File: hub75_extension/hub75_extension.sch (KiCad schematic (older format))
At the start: 23 parts

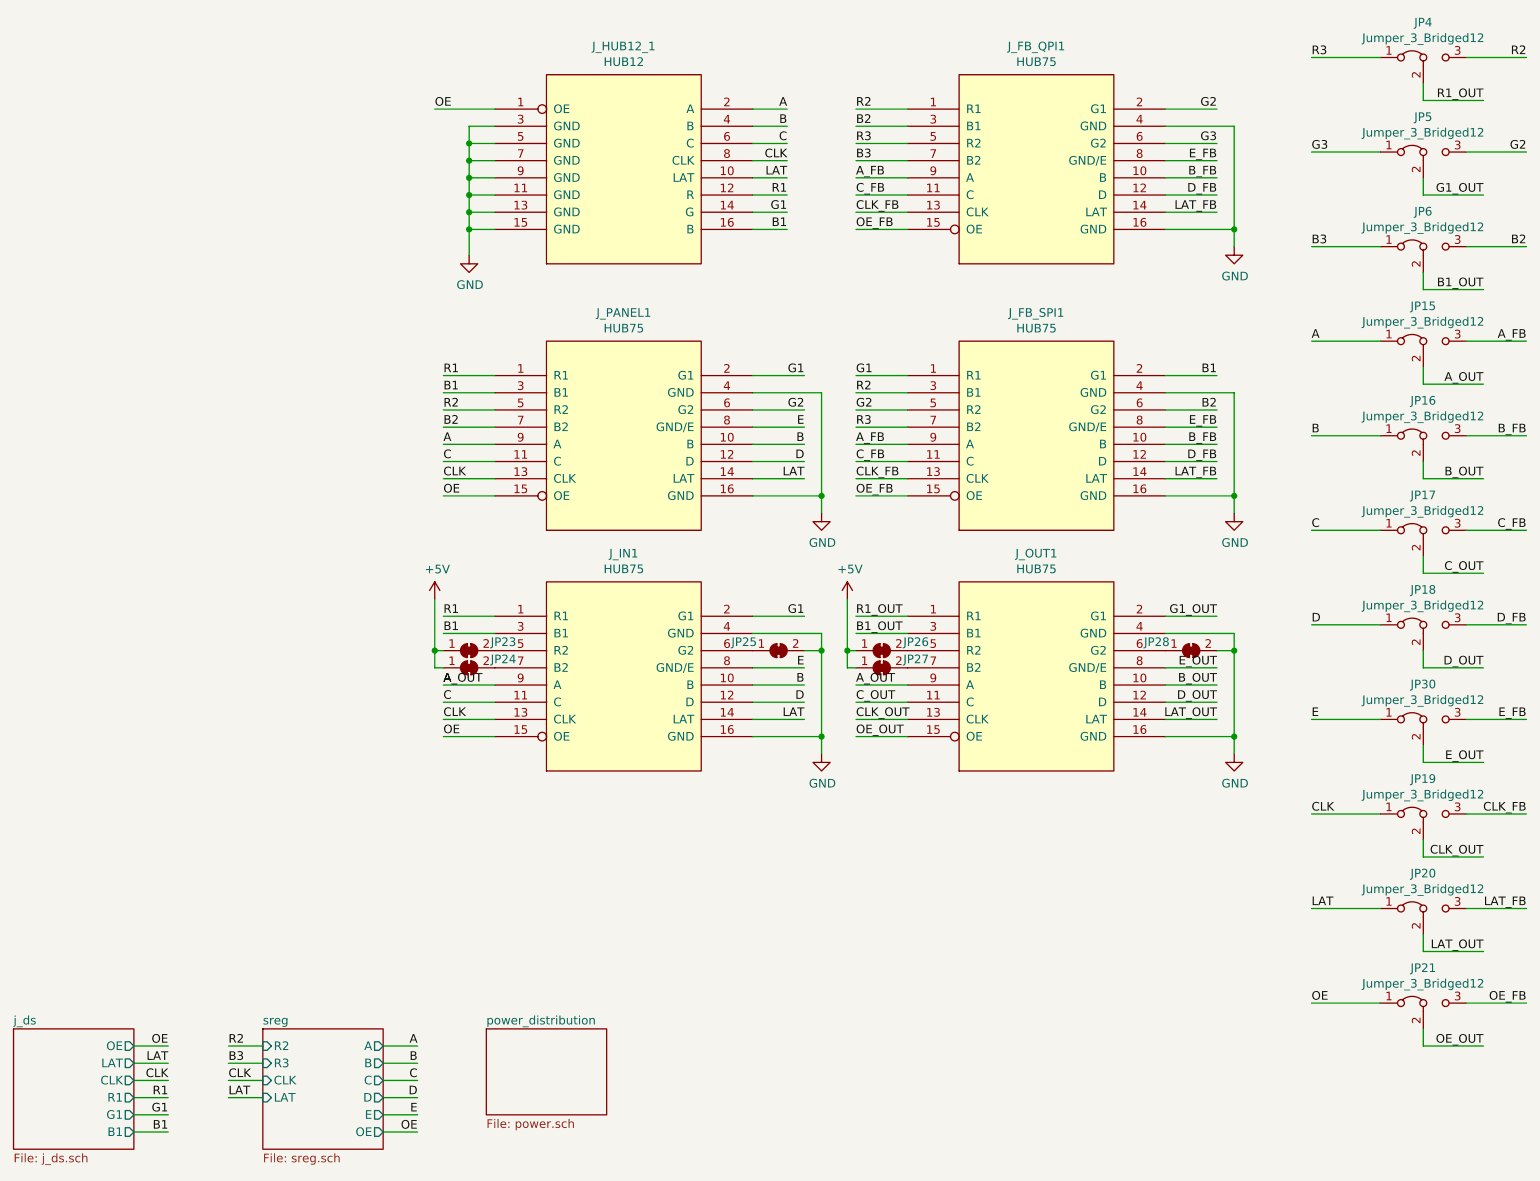
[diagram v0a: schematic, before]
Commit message: Refactor HUB75 connectors to their own sheet
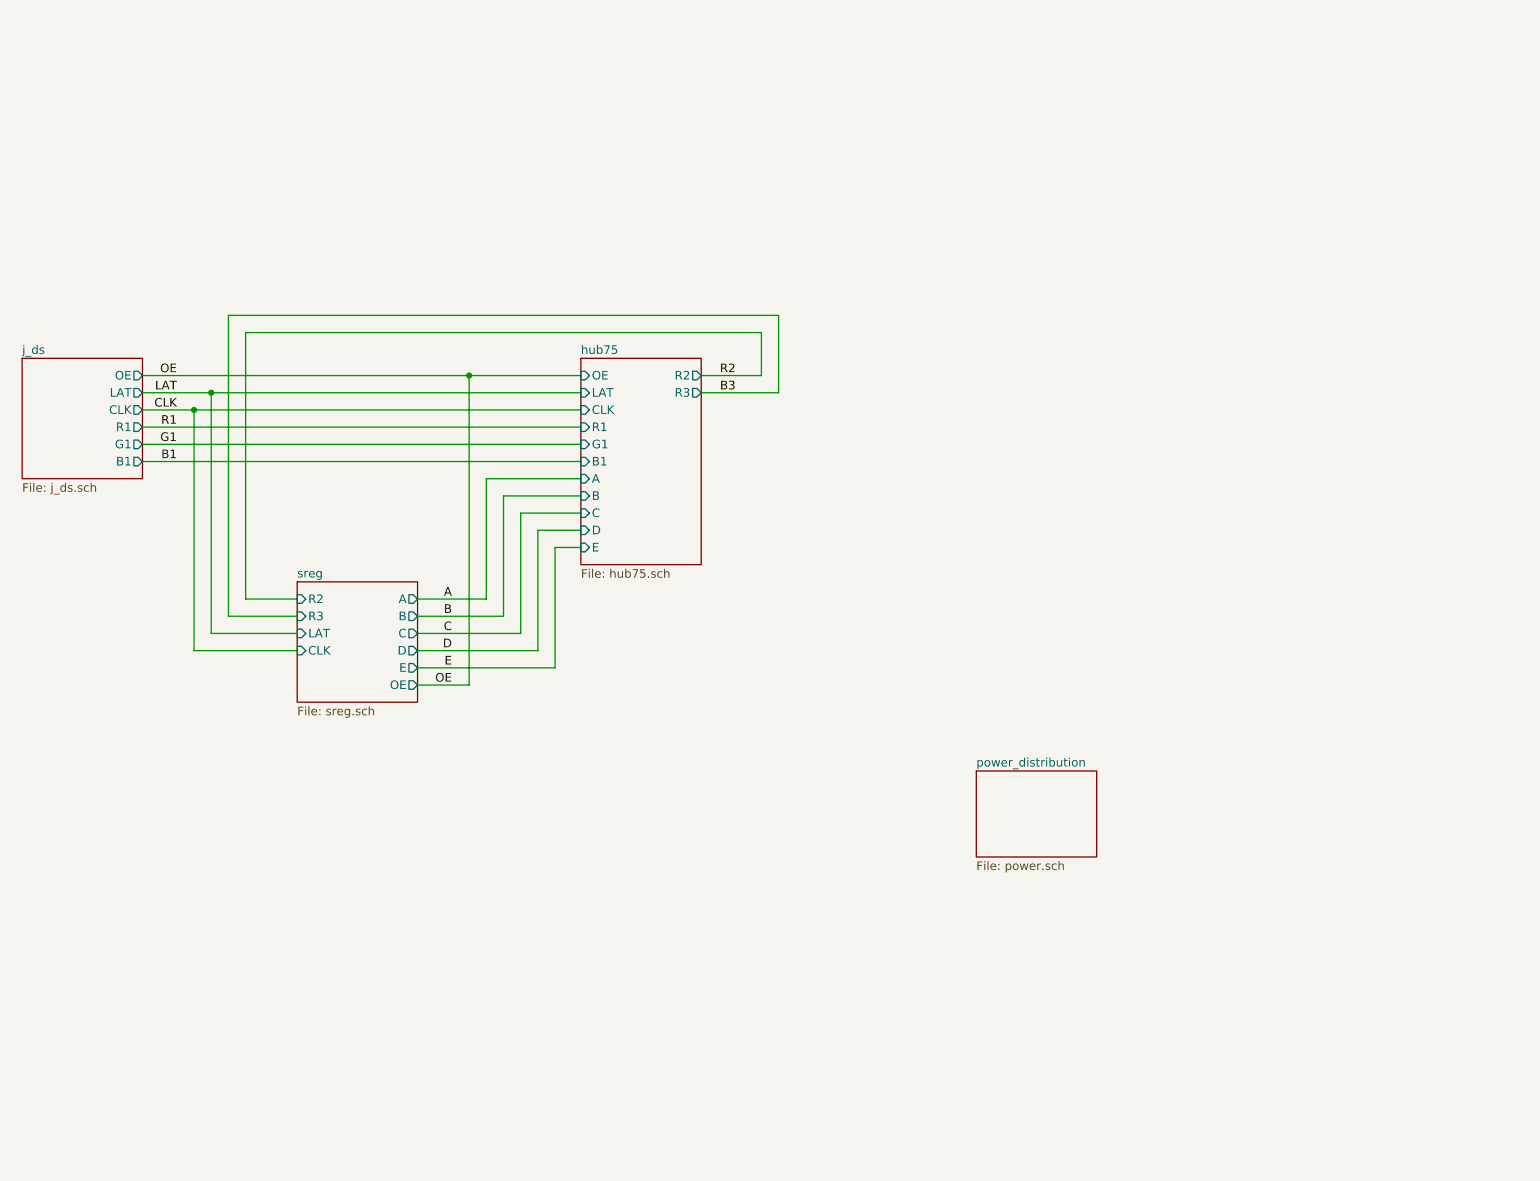
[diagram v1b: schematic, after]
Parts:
- removed JP15, JP16, JP17, JP18, JP19, JP20, JP21, JP30, JP4, JP5, JP6: Jumper_3_Bridged12, Connector_PinHeader_2.54mm:PinHeader_1x03_P2.54mm_Vertical, symbol Jumper:Jumper_3_Bridged12
- removed JP23, JP24, JP25, JP26, JP27, JP28: SolderJumper_2_Bridged, Jumper:SolderJumper-2_P1.3mm_Bridged2Bar_RoundedPad1.0x1.5mm, symbol Jumper:SolderJumper_2_Bridged
- removed J_FB_QPI1, J_FB_SPI1, J_IN1, J_OUT1: HUB75, Connector_IDC:IDC-Header_2x08_P2.54mm_Vertical, symbol HUB75:HUB75
- removed J_HUB12_1: HUB12, Connector_PinSocket_2.54mm:PinSocket_2x08_P2.54mm_Vertical, symbol HUB75:HUB12
- removed J_PANEL1: HUB75, Connector_PinSocket_2.54mm:PinSocket_2x08_P2.54mm_Vertical, symbol HUB75:HUB75
